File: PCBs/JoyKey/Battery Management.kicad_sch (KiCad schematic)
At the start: 0 parts

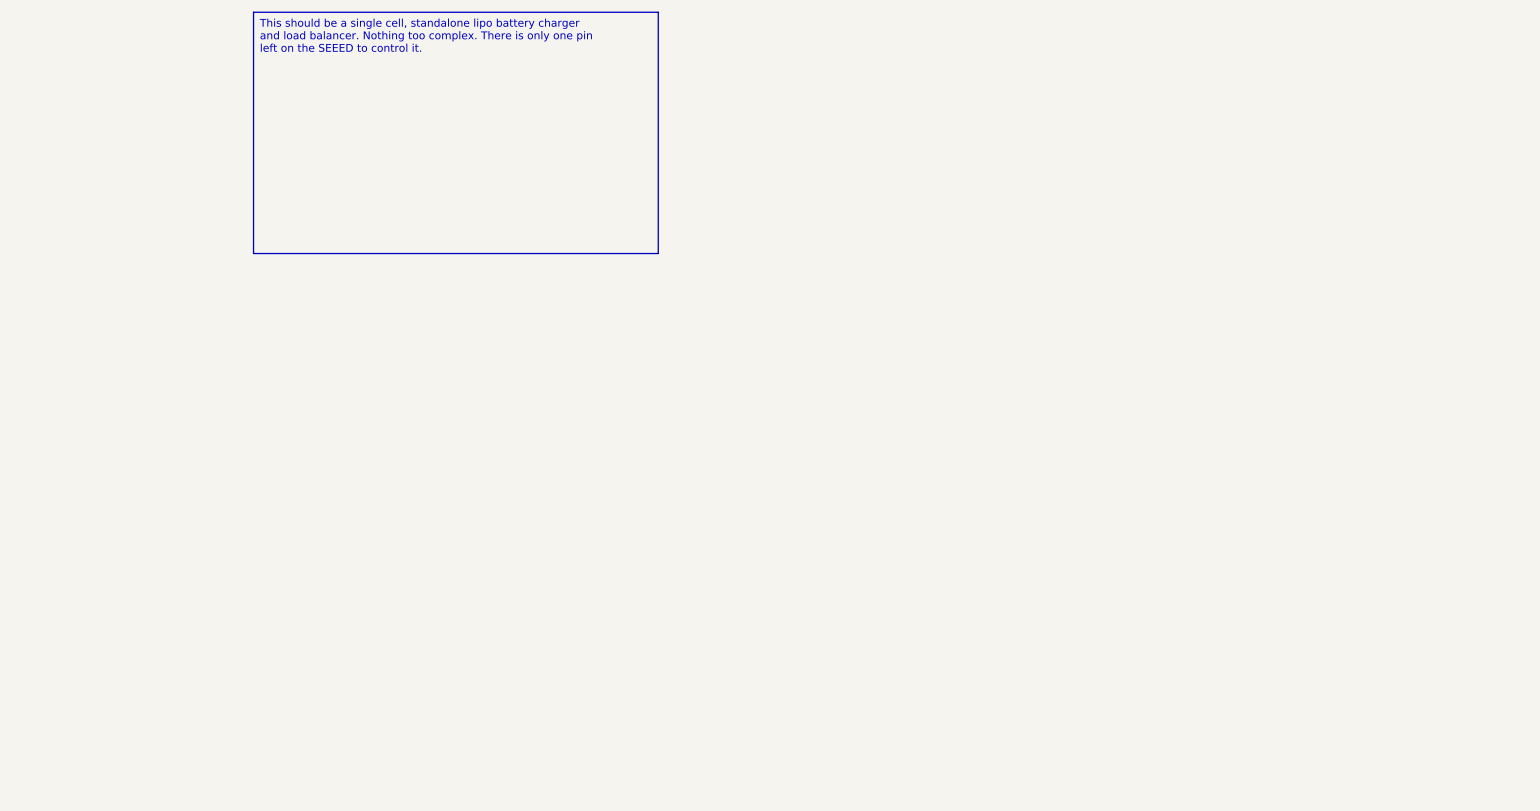
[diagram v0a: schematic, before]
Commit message: Added battery management
This is the placeholder circuit taken from one of my robot designs. I need to find cheaper and simpler chips. I do NOT need batter power path management due to the xiao being the source and drain at the same time. Something like the Adafruit Feather design.
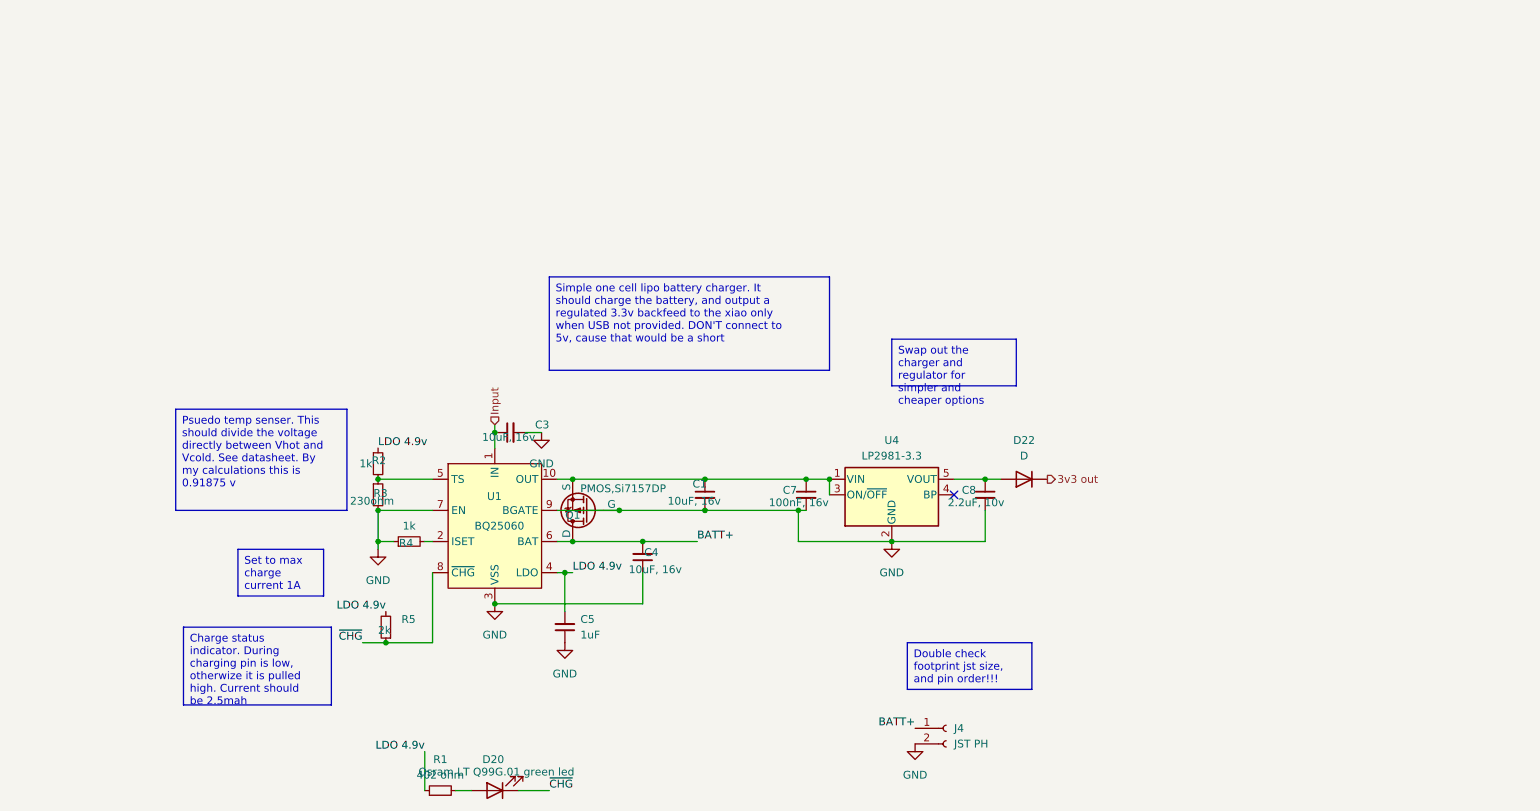
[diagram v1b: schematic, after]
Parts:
- added C1, C3, C4: 10uF, 16v, Capacitor_SMD:C_0603_1608Metric_Pad1.08x0.95mm_HandSolder, symbol Device:C_Small
- added C5: 1uF, Capacitor_SMD:C_0603_1608Metric_Pad1.08x0.95mm_HandSolder, symbol Device:C_Small
- added C7: 100nF, 16v, Capacitor_SMD:C_0402_1005Metric, symbol Device:C_Small
- added C8: 2.2uF, 10v, Capacitor_SMD:C_0402_1005Metric, symbol Device:C_Small
- added D20: Osram LT Q99G.01 green led, LED_SMD:LED_0603_1608Metric_Pad1.05x0.95mm_HandSolder, symbol Device:LED
- added D22: D, symbol Device:D
- added J4: JST PH, symbol Connector:Conn_01x02_Socket
- added Q1: PMOS,Si7157DP, Package_DFN_QFN:PQFN-8-EP_6x5mm_P1.27mm_Generic, symbol Simulation_SPICE:PMOS
- added R1: 402 ohm, Resistor_SMD:R_0603_1608Metric, symbol Device:R_Small
- added R2, R4: 1k, Resistor_SMD:R_0603_1608Metric_Pad0.98x0.95mm_HandSolder, symbol Device:R_Small
- added R3: 230ohm, Resistor_SMD:R_0603_1608Metric_Pad0.98x0.95mm_HandSolder, symbol Device:R_Small
- added R5: 2k, Resistor_SMD:R_0603_1608Metric_Pad0.98x0.95mm_HandSolder, symbol Device:R_Small
- added U1: BQ25060, custom_Power:WSON-10-1EP_2x3mm_P0.5mm_EP0.84x2.4mm_ThermalVias_0.3mm, symbol custom_Battery_Management:BQ25060
- added U4: LP2981-3.3, Package_TO_SOT_SMD:SOT-23-5, symbol Regulator_Linear:LP2985-3.3
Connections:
- new net: C8.1, D22.2 (A), U4.5 (VOUT)
- new net: C1.1, C7.1, Q1.1 (S), Q1.2 (S), Q1.3 (S), U1.10 (OUT), U4.1 (VIN), U4.3 (ON/~{OFF})
- new net: D20.2 (A), R1.2
- new net: R2.2, R3.1, U1.5 (TS)
- new net: R4.2, U1.2 (ISET)
- new net 3v3 out: D22.1 (K)
- new net BATT+: C4.2, J4.1 (Pin_1), Q1.5 (D), U1.6 (BAT)
- new net GND: C1.2, C3.2, C4.1, C5.1, C7.2, C8.2, J4.2 (Pin_2), Q1.4 (G), R3.2, R4.1, U1.11 (VSS), U1.3 (VSS), U1.7 (EN), U1.9 (BGATE), U4.2 (GND)
- new net Input: C3.1, U1.1 (IN)
- new net LDO 4.9v: C5.2, R1.1, R2.1, R5.2, U1.4 (LDO)
- new net ~{CHG}: D20.1 (K), R5.1, U1.8 (~{CHG})
- no-connect marks 0 -> 1

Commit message: Assigned footprints for batt management
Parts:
- D22: footprint (none) -> Diode_SMD:D_0805_2012Metric
- J4: footprint (none) -> Connector_JST:JST_PH_S2B-PH-SM4-TB_1x02-1MP_P2.00mm_Horizontal
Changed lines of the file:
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@@
 		(exclude_from_sim no)
 		(at 180.34 83.82 0)
-		(size 20.32 7.62)
+		(size 20.32 11.43)
 		(stroke
 			(width 0)
@@
 			)
 		)
-		(property "Footprint" ""
+		(property "Footprint" "Connector_JST:JST_PH_S2B-PH-SM4-TB_1x02-1MP_P2.00mm_Horizontal"
 			(at 189.23 147.32 0)
 			(effects
@@
 			)
 		)
-		(property "Footprint" ""
+		(property "Footprint" "Diode_SMD:D_0805_2012Metric"
 			(at 201.93 106.68 0)
 			(effects

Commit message: Updated SMD Resistor size to 0805
I don't want to use small resistors on this project, too much of a hassle.
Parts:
- C1, C3, C4, C5: footprint Capacitor_SMD:C_0603_1608Metric_Pad1.08x0.95mm_HandSolder -> Capacitor_SMD:C_0805_2012Metric
- C7, C8: footprint Capacitor_SMD:C_0402_1005Metric -> Capacitor_SMD:C_0805_2012Metric
- R1: footprint Resistor_SMD:R_0603_1608Metric -> Resistor_SMD:R_0805_2012Metric
- R2, R3, R4, R5: footprint Resistor_SMD:R_0603_1608Metric_Pad0.98x0.95mm_HandSolder -> Resistor_SMD:R_0805_2012Metric
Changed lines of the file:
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@@
 			)
 		)
-		(property "Footprint" "Capacitor_SMD:C_0402_1005Metric"
+		(property "Footprint" "Capacitor_SMD:C_0805_2012Metric"
 			(at 195.58 109.22 0)
 			(effects
@@
 			)
 		)
-		(property "Footprint" "Capacitor_SMD:C_0603_1608Metric_Pad1.08x0.95mm_HandSolder"
+		(property "Footprint" "Capacitor_SMD:C_0805_2012Metric"
 			(at 139.7 119.38 0)
 			(effects
@@
 			)
 		)
-		(property "Footprint" "Capacitor_SMD:C_0603_1608Metric_Pad1.08x0.95mm_HandSolder"
+		(property "Footprint" "Capacitor_SMD:C_0805_2012Metric"
 			(at 149.86 109.22 0)
 			(effects
@@
 			)
 		)
-		(property "Footprint" "Capacitor_SMD:C_0402_1005Metric"
+		(property "Footprint" "Capacitor_SMD:C_0805_2012Metric"
 			(at 166.37 109.22 0)
 			(effects
@@
 			)
 		)
-		(property "Footprint" "Resistor_SMD:R_0603_1608Metric"
+		(property "Footprint" "Resistor_SMD:R_0805_2012Metric"
 			(at 106.68 157.48 0)
 			(effects
@@
 			)
 		)
-		(property "Footprint" "Resistor_SMD:R_0603_1608Metric_Pad0.98x0.95mm_HandSolder"
+		(property "Footprint" "Resistor_SMD:R_0805_2012Metric"
 			(at 97.79 130.81 0)
 			(effects
@@
 			)
 		)
-		(property "Footprint" "Resistor_SMD:R_0603_1608Metric_Pad0.98x0.95mm_HandSolder"
+		(property "Footprint" "Resistor_SMD:R_0805_2012Metric"
 			(at 96.52 109.22 0)
 			(effects
@@
 			)
 		)
-		(property "Footprint" "Capacitor_SMD:C_0603_1608Metric_Pad1.08x0.95mm_HandSolder"
+		(property "Footprint" "Capacitor_SMD:C_0805_2012Metric"
 			(at 127 130.81 0)
 			(effects
@@
 			)
 		)
-		(property "Footprint" "Resistor_SMD:R_0603_1608Metric_Pad0.98x0.95mm_HandSolder"
+		(property "Footprint" "Resistor_SMD:R_0805_2012Metric"
 			(at 96.52 104.14 0)
 			(effects
@@
 			)
 		)
-		(property "Footprint" "Capacitor_SMD:C_0603_1608Metric_Pad1.08x0.95mm_HandSolder"
+		(property "Footprint" "Capacitor_SMD:C_0805_2012Metric"
 			(at 118.11 99.06 0)
 			(effects
@@
 			)
 		)
-		(property "Footprint" "Resistor_SMD:R_0603_1608Metric_Pad0.98x0.95mm_HandSolder"
+		(property "Footprint" "Resistor_SMD:R_0805_2012Metric"
 			(at 101.6 116.84 0)
 			(effects

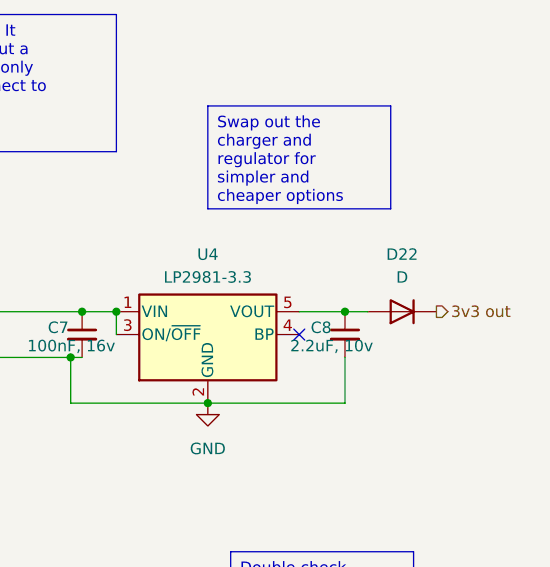
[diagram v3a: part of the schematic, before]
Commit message: Switched output diode to known model
This is a schottkey diode that I have worked with before and I know its low dropout and quick reacting
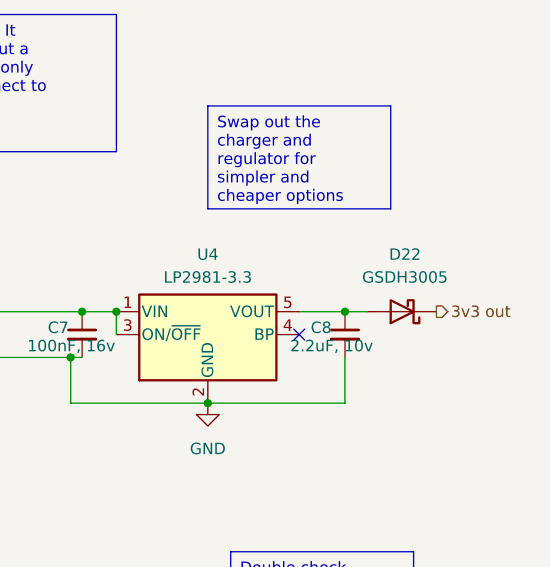
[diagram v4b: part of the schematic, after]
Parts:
- removed D22: D, Diode_SMD:D_0805_2012Metric, symbol Device:D
- added D22: GSDH3005, Diode_SMD:D_0402_1005Metric, symbol Device:D_Schottky
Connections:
- net 3v3 out: now also D22.1 (K)
- net at C8.1, U4.5 (VOUT): now also D22.2 (A)
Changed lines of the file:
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@@
-	)
-	(symbol
-		(lib_id "Device:D")
-		(at 201.93 106.68 180)
-		(unit 1)
-		(exclude_from_sim no)
-		(in_bom yes)
-		(on_board yes)
-		(dnp no)
-		(fields_autoplaced yes)
-		(property "Reference" "D22"
-			(at 201.93 100.33 0)
-			(effects
-				(font
-					(size 1.27 1.27)
-				)
-			)
-		)
-		(property "Value" "D"
-			(at 201.93 102.87 0)
-			(effects
-				(font
-					(size 1.27 1.27)
-				)
-			)
-		)
-		(property "Footprint" "Diode_SMD:D_0805_2012Metric"
-			(at 201.93 106.68 0)
-			(effects
-				(font
-					(size 1.27 1.27)
-				)
-				(hide yes)
-			)
-		)
-		(property "Datasheet" "~"
-			(at 201.93 106.68 0)
-			(effects
-				(font
-					(size 1.27 1.27)
-				)
-				(hide yes)
-			)
-		)
-		(property "Description" "Diode"
-			(at 201.93 106.68 0)
-			(effects
-				(font
-					(size 1.27 1.27)
-				)
-				(hide yes)
-			)
-		)
-		(property "Sim.Device" "D"
-			(at 201.93 106.68 0)
-			(effects
-				(font
-					(size 1.27 1.27)
-				)
-				(hide yes)
-			)
-		)
-		(property "Sim.Pins" "1=K 2=A"
-			(at 201.93 106.68 0)
-			(effects
-				(font
-					(size 1.27 1.27)
-				)
-				(hide yes)
-			)
-		)
-		(pin "1"
-		)
-		(pin "2"
-		)
-		(instances
-			(project ""
-				(path "/7995ec7a-c14b-437e-b354-3eb74052b7cb/ac250670-848c-4fb5-87be-316f940b1e65"
-					(reference "D22")
-					(unit 1)
-				)
-			)
-		)
 	)
 	(symbol
@@
 					(unit 1)
 				)
+			)
+		)
+	)
+	(symbol
+		(lib_id "Device:D_Schottky")
+		(at 201.93 106.68 180)
+		(unit 1)
+		(exclude_from_sim no)
+		(in_bom yes)
+		(on_board yes)
+		(dnp no)
+		(fields_autoplaced yes)
+		(property "Reference" "D22"
+			(at 202.2475 100.33 0)
+			(effects
+				(font
+					(size 1.27 1.27)
+				)
+			)
+		)
+		(property "Value" "GSDH3005"
+			(at 202.2475 102.87 0)
+			(effects
+				(font
+					(size 1.27 1.27)
+				)
+			)
+		)
+		(property "Footprint" "Diode_SMD:D_0402_1005Metric"
+			(at 201.93 106.68 0)
+			(effects
+				(font
+					(size 1.27 1.27)
+				)
+				(hide yes)
+			)
+		)
+		(property "Datasheet" "~"
+			(at 201.93 106.68 0)
+			(effects
+				(font
+					(size 1.27 1.27)
+				)
+				(hide yes)
+			)
+		)
+		(property "Description" "Schottky diode"
+			(at 201.93 106.68 0)
+			(effects
+				(font
+					(size 1.27 1.27)
+				)
+				(hide yes)
+			)
+		)
+		(property "Sim.Device" "D"
+			(at 201.93 106.68 0)
+			(effects
+				(font
+					(size 1.27 1.27)
+				)
+				(hide yes)
+			)
+		)
+		(property "Sim.Pins" "1=K 2=A"
+			(at 201.93 106.68 0)
+			(effects
+				(font
+					(size 1.27 1.27)
+				)
+				(hide yes)
+			)
+		)
+		(property "LCSC" "C2837790"
+			(at 200.9774 104.14 0)
+			(effects
+				(font
+					(size 1.27 1.27)
+				)
+				(hide yes)
+			)
+		)
+		(pin "2"
+		)
+		(pin "1"
+		)
+		(instances
+			(project "JoyKey"
+				(path "/7995ec7a-c14b-437e-b354-3eb74052b7cb/ac250670-848c-4fb5-87be-316f940b1e65"
+					(reference "D22")
+					(unit 1)
+				)

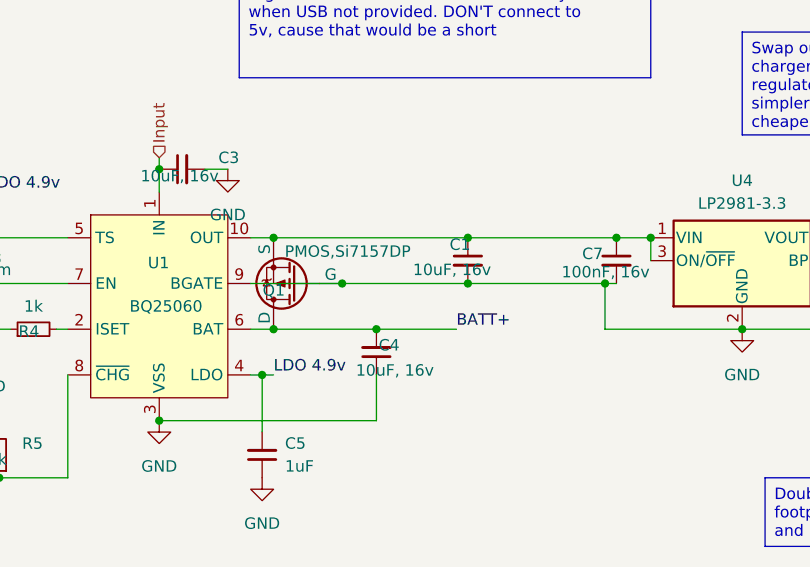
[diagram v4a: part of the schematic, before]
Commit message: Fixed short between battery gate and ground
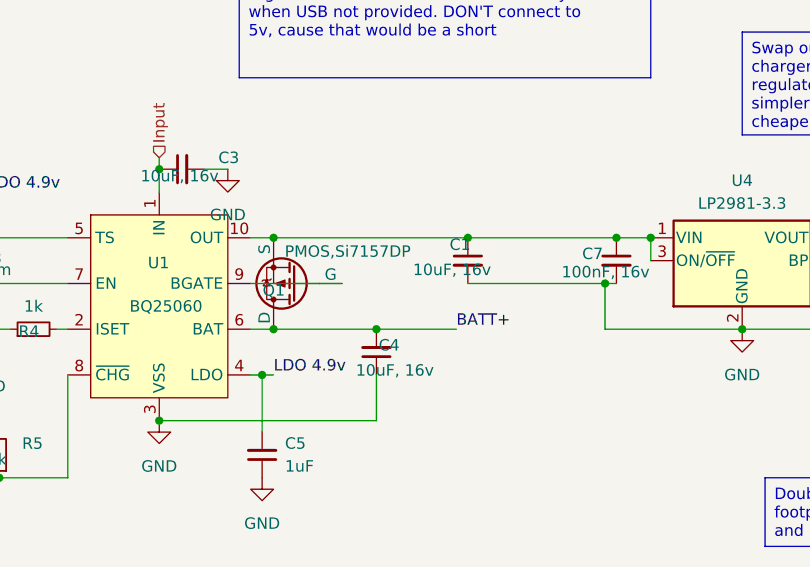
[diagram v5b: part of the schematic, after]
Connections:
- net GND: no longer Q1.4 (G), U1.9 (BGATE)
- new net: Q1.4 (G), U1.9 (BGATE)
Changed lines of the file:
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@@
-	)
-	(junction
-		(at 149.86 111.76)
-		(diameter 0)
-		(color 0 0 0 0)
 	)
 	(junction
@@
 	)
 	(junction
-		(at 135.89 111.76)
-		(diameter 0)
-		(color 0 0 0 0)
-	)
-	(junction
 		(at 128.27 116.84)
 		(diameter 0)
@@
 		)
 		(stroke
-			(width 0)
-			(type default)
-		)
-	)
-	(wire
-		(pts
-			(xy 135.89 111.76) (xy 149.86 111.76)
-		)
-		(stroke
